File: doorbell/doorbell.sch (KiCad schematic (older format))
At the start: 26 parts, among them J1 39700-0012, K1 G6E-134P-US DC12, T1 CT05-1000, U1 LM2575-12WT, U2 LM358, U3 COM-16473 (NA555)

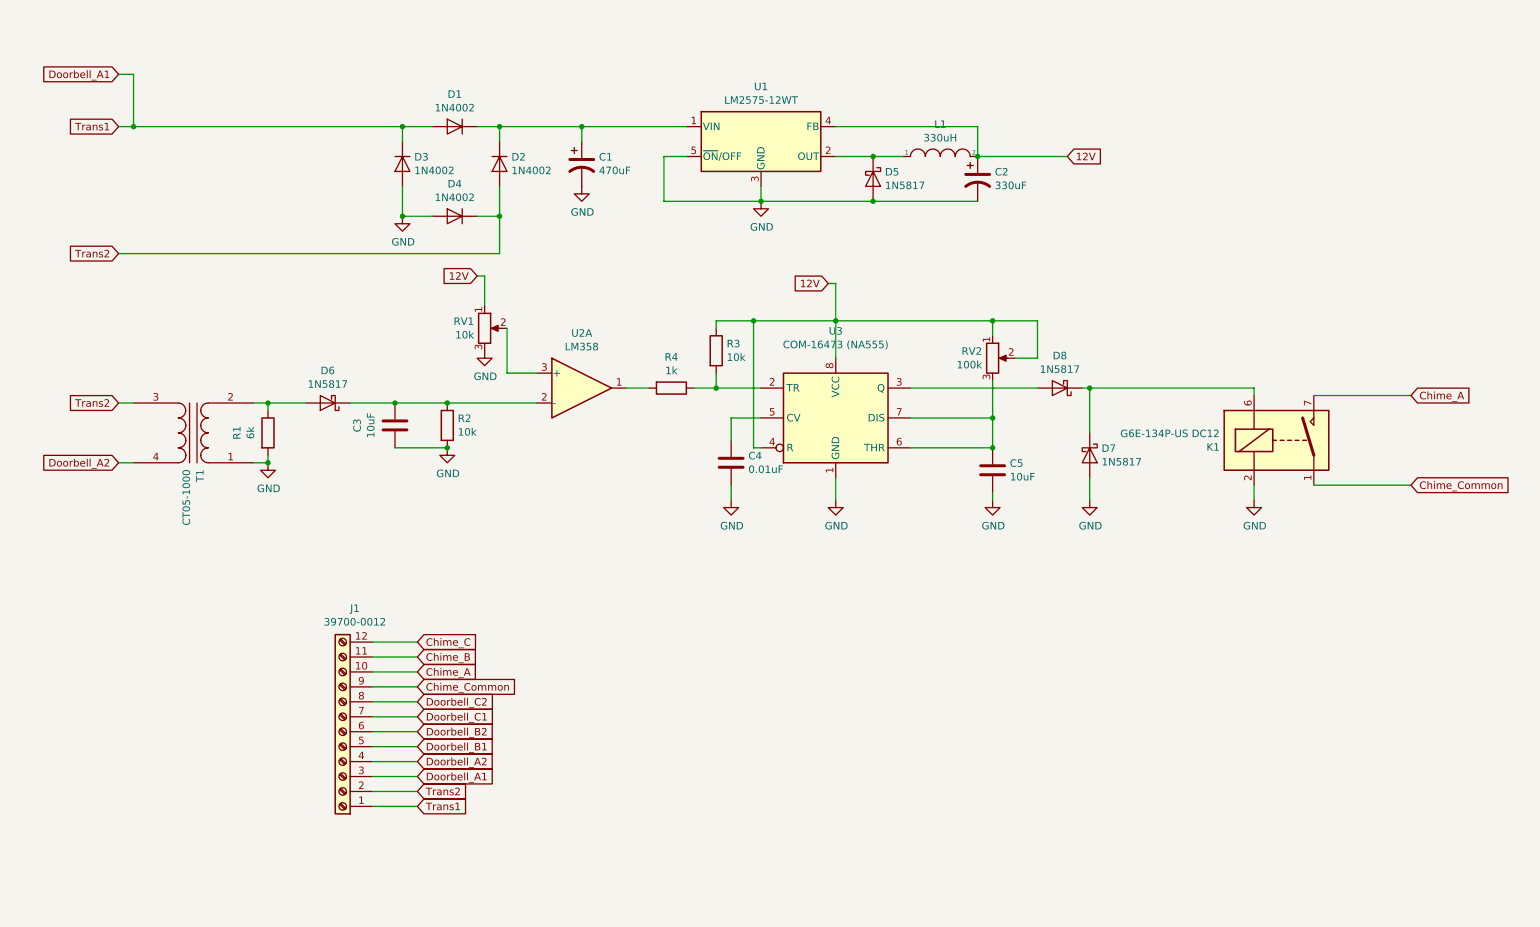
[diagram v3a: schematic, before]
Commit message: Updating schematic to include all three CTs
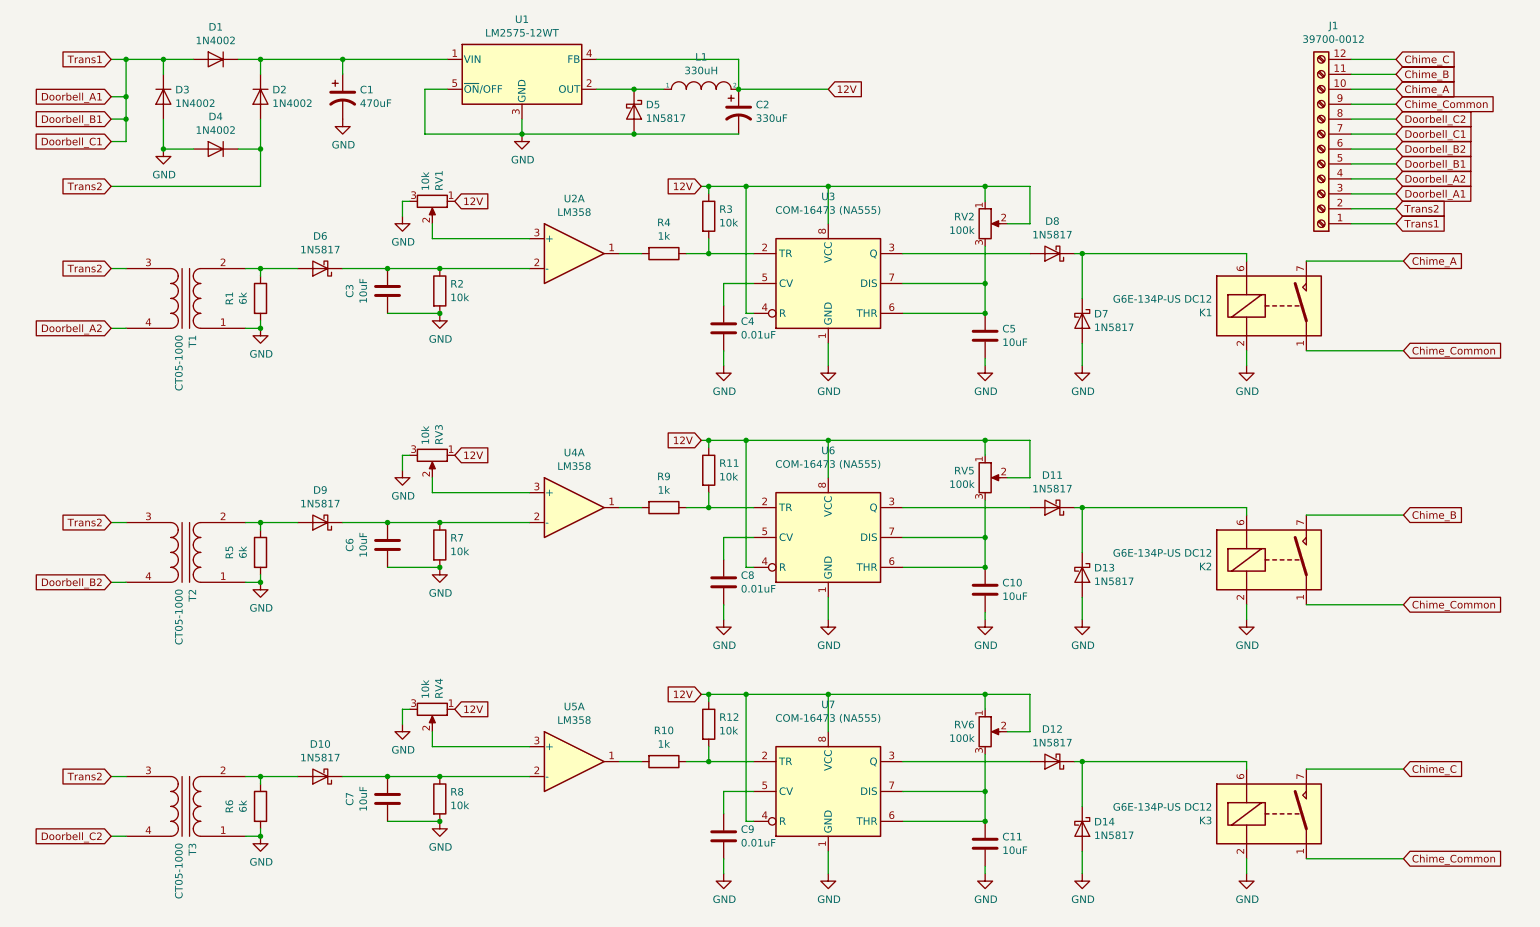
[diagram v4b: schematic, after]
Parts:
- added C10, C11, C6, C7: 10uF, symbol Device:C
- added C8, C9: 0.01uF, symbol Device:C
- added D10, D11, D12, D13, D14, D9: 1N5817, Diode_THT:D_DO-41_SOD81_P10.16mm_Horizontal, symbol Diode:1N5817
- added K2, K3: G6E-134P-US DC12, Relay_THT:Relay_SPDT_Omron_G6E, symbol Relay:DIPxx-1Axx-11x
- added R10, R9: 1k, symbol Device:R
- added R11, R12, R7, R8: 10k, symbol Device:R
- added R5, R6: 6k, symbol Device:R
- added RV3, RV4: 10k, symbol Device:R_POT
- added RV5, RV6: 100k, symbol Device:R_POT
- added T2, T3: CT05-1000, symbol Device:Transformer_1P_1S
- added U4, U5: LM358, Package_DIP:DIP-8_W7.62mm, symbol Amplifier_Operational:LM358
- added U6, U7: COM-16473 (NA555), Package_DIP:DIP-8_W7.62mm, symbol Timer:LM555
- K1: footprint Relay_THT:Relay_StandexMeder_DIP_LowProfile -> Relay_THT:Relay_SPDT_Omron_G6E
- U1: footprint Package_TO_SOT_SMD:TO-263-5_TabPin3 -> Package_TO_SOT_THT:TO-262-5_Vertical
- U2, U3: footprint (none) -> Package_DIP:DIP-8_W7.62mm
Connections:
- net Doorbell_B1 is gone; now on net Doorbell_A1: J1.5 (Pin_5)
- net Doorbell_C1 is gone; now on net Doorbell_A1: J1.7 (Pin_7)
- net 12V: now also R11.1, R12.1, RV3.1, RV4.1, RV5.1, RV5.2, RV6.1, RV6.2, U6.4 (R), U6.8 (VCC), U7.4 (R), U7.8 (VCC)
- net Chime_B: now also K2.7, K2.8
- net Chime_C: now also K3.7, K3.8
- net Chime_Common: now also K2.1, K2.14, K3.1, K3.14
- net Doorbell_B2: now also T2.4 (SB)
- net Doorbell_C2: now also T3.4 (SB)
- net GND: now also C10.2, C11.2, C6.2, C7.2, C8.2, C9.2, D13.2 (A), D14.2 (A), K2.2, K3.2, R5.2, R6.2, R7.2, R8.2, RV3.3, RV4.3, T2.1 (AA), T3.1 (AA), U6.1 (GND), U7.1 (GND)
- net Trans2: now also T2.3 (SA), T3.3 (SA)
- new net: D9.2 (A), R5.1, T2.2 (AB)
- new net: C6.1, D9.1 (K), R7.1, U4.2 (-)
- new net: R11.2, R9.1, U6.2 (TR)
- new net: D11.2 (A), U6.3 (Q)
- new net: C8.1, U6.5 (CV)
- new net: C10.1, RV5.3, U6.6 (THR), U6.7 (DIS)
- new net: D11.1 (K), D13.1 (K), K2.6
- new net: R9.2, U4.1
- new net: RV3.2, U4.3 (+)
- new net: D10.2 (A), R6.1, T3.2 (AB)
- new net: C7.1, D10.1 (K), R8.1, U5.2 (-)
- new net: R10.1, R12.2, U7.2 (TR)
- new net: D12.2 (A), U7.3 (Q)
- new net: C9.1, U7.5 (CV)
- new net: C11.1, RV6.3, U7.6 (THR), U7.7 (DIS)
- new net: D12.1 (K), D14.1 (K), K3.6
- new net: R10.2, U5.1
- new net: RV4.2, U5.3 (+)
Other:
- moved on the sheet: C1, C2, C3, C4, C5, D1, D2, D3, D4, D5, D6, D7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
